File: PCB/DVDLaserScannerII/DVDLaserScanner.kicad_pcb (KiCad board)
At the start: 2 copper layers, 144 x 80 mm, 83 parts, among them Q1 Q_NMOS_GDS, SW1 BUT, U1 MCP4922-E/SL, U10 Con45, U11 Con45, U13 TLC2274, U2 MCP4922-E/SL, U3 ARDUINO_MICRO, U4 TCA0372_DWG, U5 TCA0372_DWG, U6 TCA0372_DWG, U7 MCP6002, U8 MCP4922-E/SL, U9 TLC2274, X1 MountPad3, X2 MountPad3, X3 MountPad3, X4 MountPad3, X5 PAD, X6 PAD, X7 PAD

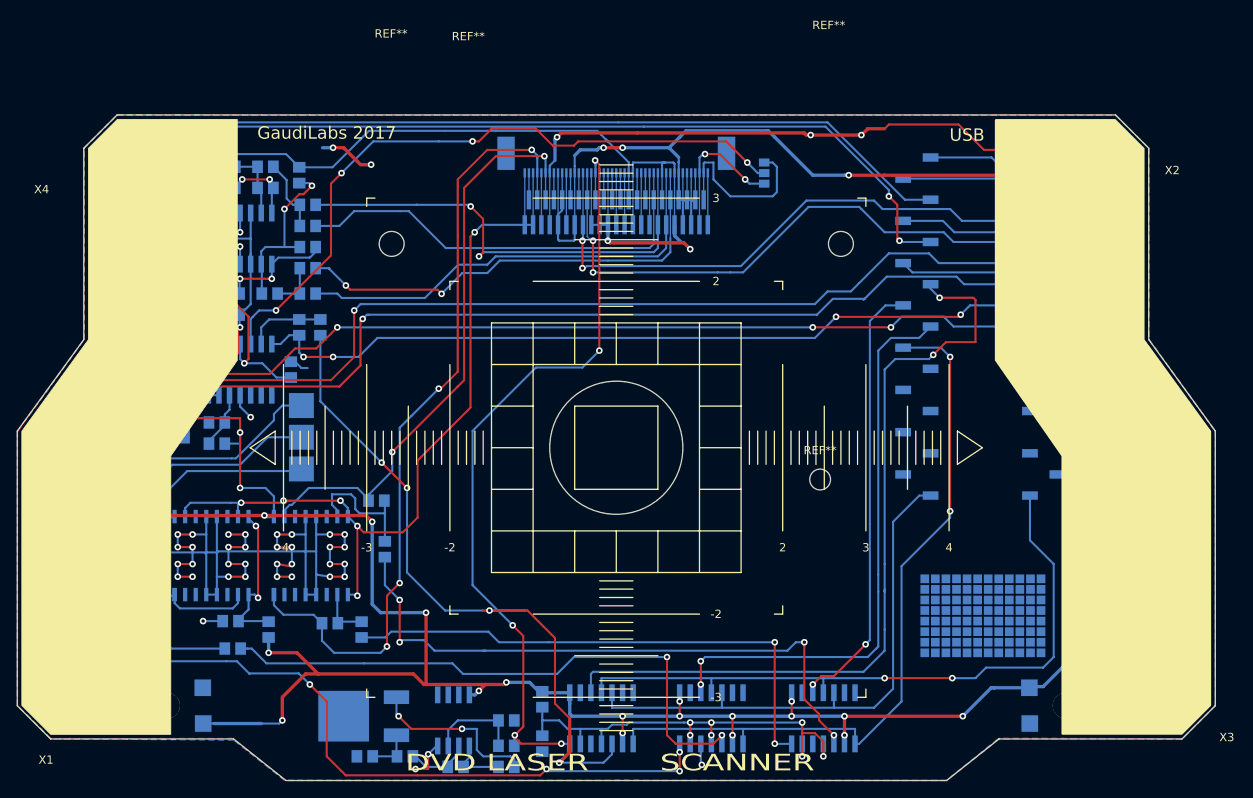
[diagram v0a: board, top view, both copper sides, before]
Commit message: pcb: Remove left and right outlines from front silkscreen
Update pcb and regenerate gerbers
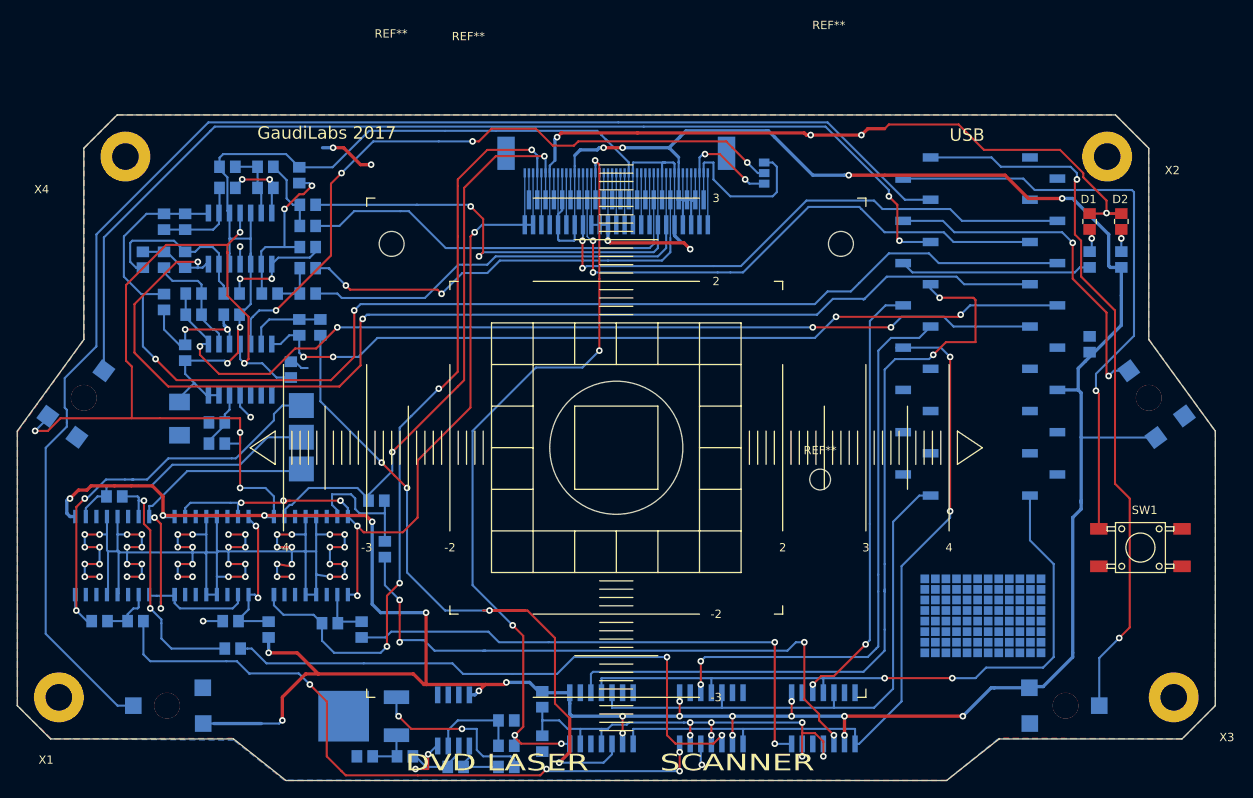
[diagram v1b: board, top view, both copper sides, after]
